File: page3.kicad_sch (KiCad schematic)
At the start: 27 parts, among them U23 CD4094

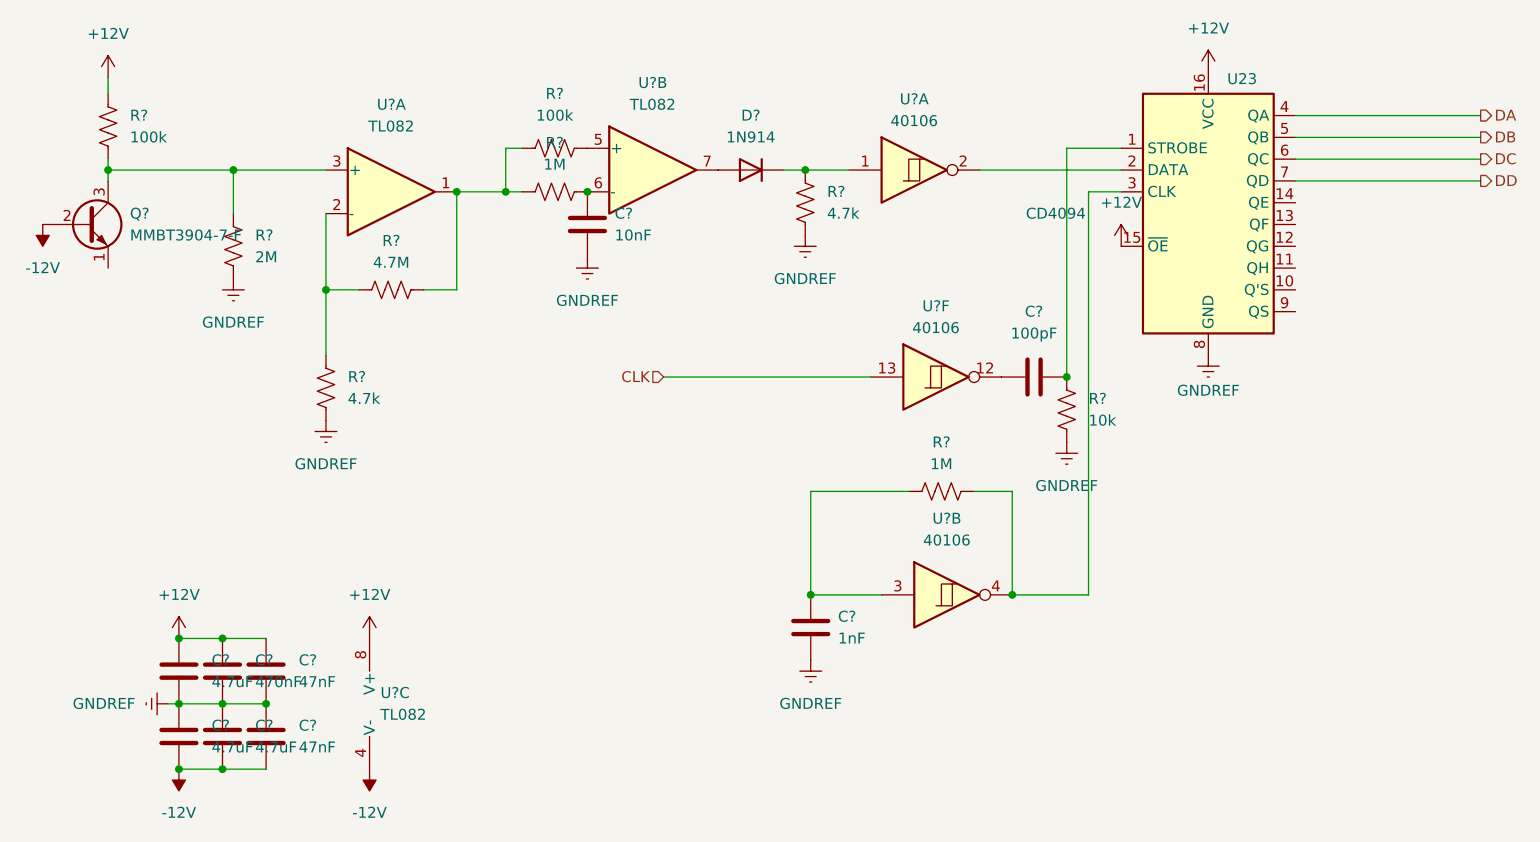
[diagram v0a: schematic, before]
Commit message: created pcb file, placed parts
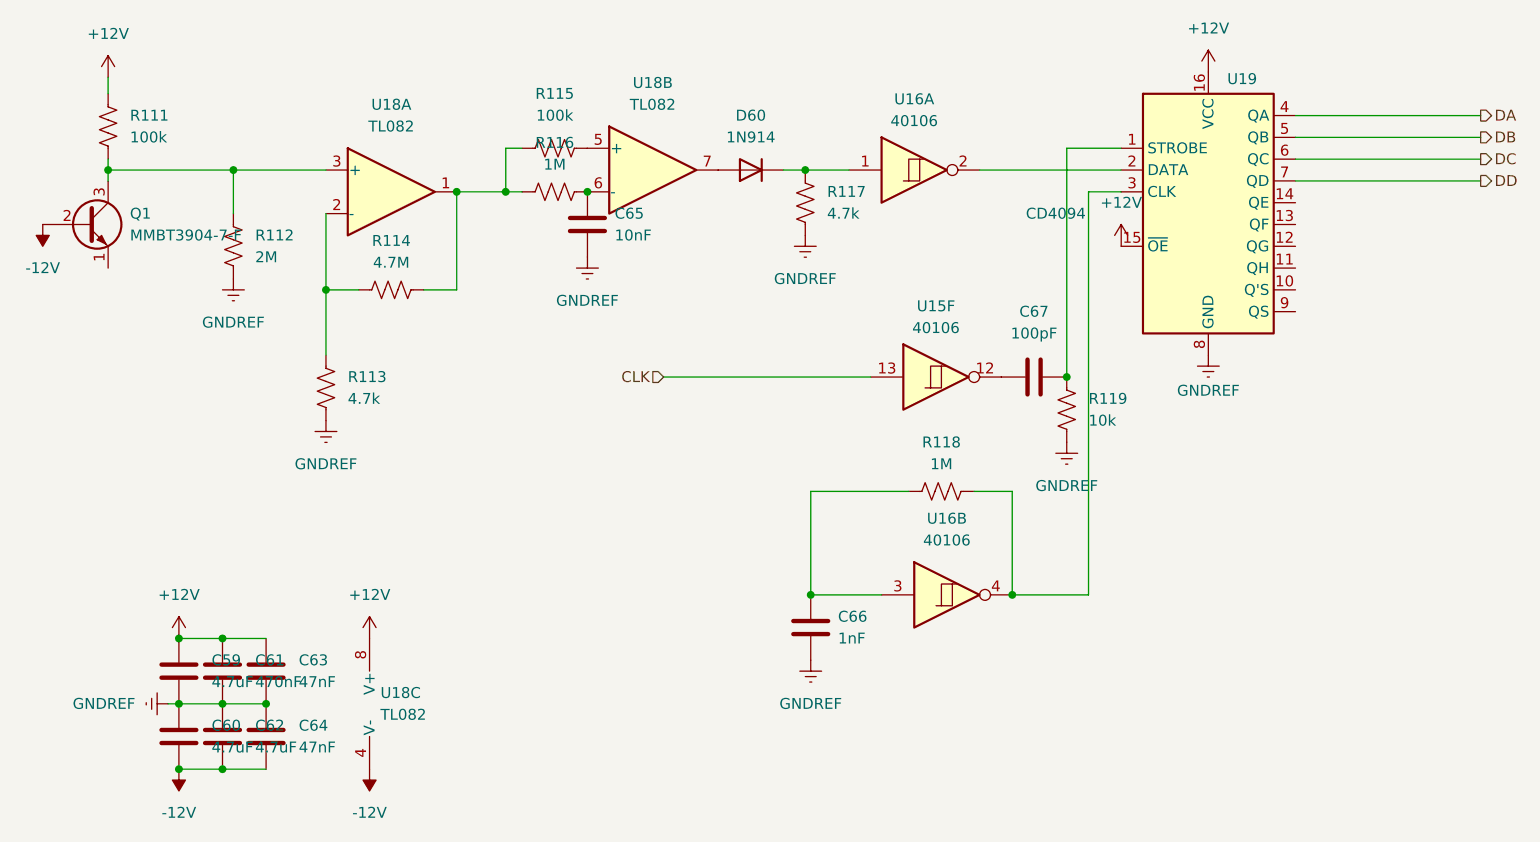
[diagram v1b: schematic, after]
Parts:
- gave numbers to parts that had none: 23
- renumbered U23 to U19

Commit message: routing and placing
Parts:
- removed U15: 40106, Package_SO:SOIC-14_3.9x8.7mm_P1.27mm, symbol 4xxx:40106
- added unit 4 of U16
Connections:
- net CLK: now also U16.9
- net at C67.2: now also U16.8
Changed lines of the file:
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@@
+    )
+  )
+  (symbol (lib_id "4xxx:40106") (at 156.845 102.235 0) (unit 4)
+    (in_bom yes) (on_board yes) (dnp no) (fields_autoplaced)
+    (property "Reference" "U16" (at 156.845 93.345 0)
+      (effects (font (size 1.27 1.27)))
+    )
+    (property "Value" "40106" (at 156.845 95.885 0)
+      (effects (font (size 1.27 1.27)))
+    )
+    (property "Footprint" "Package_SO:SOIC-14_3.9x8.7mm_P1.27mm" (at 156.845 102.235 0)
+      (effects (font (size 1.27 1.27)) hide)
+    )
+    (property "Datasheet" "https://assets.nexperia.com/documents/data-sheet/HEF40106B.pdf" (at 156.845 102.235 0)
+      (effects (font (size 1.27 1.27)) hide)
+    )
+    (pin "1")
+    (pin "2")
+    (pin "3")
+    (pin "4")
+    (pin "5")
+    (pin "6")
+    (pin "8")
+    (pin "9")
+    (pin "10")
+    (pin "11")
+    (pin "12")
+    (pin "13")
+    (pin "14")
+    (pin "7")
+    (instances
+      (project "SoundLab16StepSequencer"
+        (path "/0a1377c9-61ff-44bc-b9df-99baf54c0c4b/0a7f3508-a968-4335-a62b-d4c2b646ff42"
+          (reference "U16") (unit 4)
+        )
+        (path "/0a1377c9-61ff-44bc-b9df-99baf54c0c4b/723e5845-6dab-4e5f-b261-119d3e558f03"
+          (reference "U16") (unit 4)
+        )
+      )
+      (project "AnalogTestBoard2"
+        (path "/6a5989ee-c5d0-4815-8576-7e34f570dc2e/fdea9e22-b4da-4f95-ae69-b8e3bce30eaf"
+          (reference "U?") (unit 4)
+        )
+      )
+      (project "SynthProj"
+        (path "/9021c97e-351f-4ed9-b393-50257df6a463/83f63f47-5f59-465e-b73f-db84e2bb89da"
+          (reference "U19") (unit 4)
+        )
+      )
     )
   )
@@
         )
       )
-    )
-  )
-  (symbol (lib_id "4xxx:40106") (at 156.845 102.235 0) (unit 6)
-    (in_bom yes) (on_board yes) (dnp no) (fields_autoplaced)
-    (property "Reference" "U15" (at 156.845 93.98 0)
-      (effects (font (size 1.27 1.27)))
-    )
-    (property "Value" "40106" (at 156.845 96.52 0)
-      (effects (font (size 1.27 1.27)))
-    )
-    (property "Footprint" "Package_SO:SOIC-14_3.9x8.7mm_P1.27mm" (at 156.845 102.235 0)
-      (effects (font (size 1.27 1.27)) hide)
-    )
-    (property "Datasheet" "https://assets.nexperia.com/documents/data-sheet/HEF40106B.pdf" (at 156.845 102.235 0)
-      (effects (font (size 1.27 1.27)) hide)
-    )
-    (pin "1")
-    (pin "2")
-    (pin "3")
-    (pin "4")
-    (pin "5")
-    (pin "6")
-    (pin "8")
-    (pin "9")
-    (pin "10")
-    (pin "11")
-    (pin "12")
-    (pin "13")
-    (pin "14")
-    (pin "7")
-    (instances
-      (project "SoundLab16StepSequencer"
-        (path "/0a1377c9-61ff-44bc-b9df-99baf54c0c4b/723e5845-6dab-4e5f-b261-119d3e558f03"
-          (reference "U15") (unit 6)
-        )
-      )
-      (project "AnalogTestBoard2"
-        (path "/6a5989ee-c5d0-4815-8576-7e34f570dc2e/ed24d926-d300-42c2-8340-a1422fc4b1b6"
-          (reference "U?") (unit 6)
-        )
-        (path "/6a5989ee-c5d0-4815-8576-7e34f570dc2e/4aa3d8e0-aa03-48c4-8c93-660db3f6c1df"
-          (reference "U?") (unit 6)
-        )
-      )
-      (project "SynthProj"
-        (path "/9021c97e-351f-4ed9-b393-50257df6a463/627a6224-0696-4472-8130-0038baa573b5"
-          (reference "U22") (unit 6)
-        )
-      )

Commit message: routed 100%
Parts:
- removed C59, C60, C62: 4.7uF, Capacitor_SMD:C_0805_2012Metric, symbol Device:C
- removed C61: 470nF, Capacitor_SMD:C_0805_2012Metric, symbol Device:C
- removed C63, C64: 47nF, Capacitor_SMD:C_0603_1608Metric, symbol Device:C
- added C50, C52: 470nF, Capacitor_SMD:C_0805_2012Metric, symbol Device:C
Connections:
- net +12V: now also C52.1
- net -12V: now also C50.2
- net GNDREF: now also C50.1, C52.2
